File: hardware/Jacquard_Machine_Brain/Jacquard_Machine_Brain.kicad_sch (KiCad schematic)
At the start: 69 parts, among them J1 Terminal Block, J15 USB_A, J16 Wurth_RJ45_LED, J2 Conn_01x08, J3 JST-SH 01x04, J4 Conn_01x02, J5 Conn_01x02, SW1 SW_DIP_x02, SW2 SW_MEC_5G, U1 R-78E5.0-1.0, U10 74AHCT1G125, U2 Teensy4.1, U3 74AHCT1G125, U4 74AHCT1G125, U5 74AHCT125, U6 AO4882, U7 74AHCT1G125, U8 74AHCT1G125, U9 PCA9306D

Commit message: sync
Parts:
- removed C6: 0.1uF, Capacitor_SMD:C_0402_1005Metric, symbol Device:C_Small
- removed JP1, JP2, JP5, JP6, JP7, JP8: SolderJumper_2_Bridged, Jumper:SolderJumper-2_P1.3mm_Bridged_RoundedPad1.0x1.5mm, symbol Jumper:SolderJumper_2_Bridged
- removed R12, R13: 4.7k, Resistor_SMD:R_0603_1608Metric, symbol Device:R_Small
- removed U5: 74AHCT125, Package_SO:TSSOP-14_4.4x5mm_P0.65mm, symbol 0_integrated_circuits:74AHCT125_Multi
- added JP1, JP2, JP5: SolderJumper_3_Bridged123, Jumper:SolderJumper-3_P1.3mm_Bridged123_RoundedPad1.0x1.5mm_NumberLabels, symbol Jumper:SolderJumper_3_Bridged123
- added R17, R18, R19, R20: 4.7k, Resistor_SMD:R_0603_1608Metric, symbol Device:R_Small
- C9: value 0.1uF -> 100pF; LCSC C1525 -> C1546; Link https://www.digikey.com/en/products/detail/samsung-electro-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 -> (none); Manu # CL05B104KO5NNNC -> 0402CG101J500NT; Manu. Samsung Electro-Mechanics -> FH (Guangdong Fenghua Advanced Tech)
- U9: LCSC (none) -> C2677369
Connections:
- net +3V3: now also JP1.2 (C), JP2.2 (C)
- net +5V: now also JP5.2 (C); no longer R15.1, R16.1
- net GATE_1: now also R4.1
- net GATE_2: now also R5.1
- net SCL_0_3.3V: now also R19.2
- net SCL_0_5V: now also R15.2
- net SCL_1: now also R18.2
- net SDA_0_3.3V: now also R20.2
- net SDA_0_5V: now also R16.2
- net SDA_1: now also R17.2
- new net: JP1.1 (A), R18.1
- new net: JP1.3 (B), R17.1
- new net: JP2.1 (A), R20.1
- new net: JP2.3 (B), R19.1
- new net: JP5.1 (A), R16.1
- new net: JP5.3 (B), R15.1
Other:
- note added: "3.3V to 5V LEVEL CONVERSION FOR SHIFT REGISTER DRIVE"
- note added: "DUAL MOSFET SWITCHES"
- note added: "GP CONTROLS"
- note added: "MOSFET GATE DRIVE"
- note added: "TEENSY 4.1"
- moved on the sheet: C10, C11, C12, C3, C4, C5, C7, C8, C9, D2, D3, D4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

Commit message: Progress check
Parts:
- removed J16: Wurth_RJ45_LED, 0_connector:Wurth_7499010211A_RJ45, symbol 0_connector:Wurth_RJ45_LED
- removed JP2, JP5: SolderJumper_3_Bridged123, Jumper:SolderJumper-3_P1.3mm_Bridged123_RoundedPad1.0x1.5mm_NumberLabels, symbol Jumper:SolderJumper_3_Bridged123
- removed SW1: SW_DIP_x02, Button_Switch_THT:SW_DIP_SPSTx02_Slide_9.78x7.26mm_W7.62mm_P2.54mm, symbol Switch:SW_DIP_x02
- removed SW2: SW_MEC_5G, Button_Switch_THT:SW_TH_Tactile_Omron_B3F-100x, symbol Switch:SW_MEC_5G
- added C6: 0.1uF, Capacitor_SMD:C_0402_1005Metric, symbol Device:C_Small
- added J200: WIZnet_J1B1211CCD_RJ45, 0_connector:WIZnet_J1B1211CCD_RJ45, symbol 0_connector:WIZnet_J1B1211CCD_RJ45
- C3: footprint Capacitor_SMD:C_0805_2012Metric_Pad1.18x1.45mm_HandSolder -> Capacitor_SMD:C_0805_2012Metric; Digikey P/N (none) -> 311-1140-1-ND; Digikey Page (none) -> https://www.digikey.com/en/products/detail/yageo/CC0805KRX7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; LCSC (none) -> C49678; Link https://www.digikey.com/en/products/detail/samsung-electro-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 -> (none); Manu # CL21B104KBCNNNC -> CC0805KRX7R9BB104; Manu. Samsung Electro-Mechanics -> YAGEO
- F1: LCSC - -> C151075
- J1: LCSC - -> C89123
- J15: LCSC (none) -> C5815125
- JP1: footprint Jumper:SolderJumper-3_P1.3mm_Bridged123_RoundedPad1.0x1.5mm_NumberLabels -> Jumper:SolderJumper-3_P1.3mm_Open_RoundedPad1.0x1.5mm; symbol Jumper:SolderJumper_3_Bridged123 -> Jumper:SolderJumper_3_Open
- R3: value 330 -> 220R; footprint Resistor_SMD:R_0805_2012Metric_Pad1.20x1.40mm_HandSolder -> Resistor_SMD:R_0805_2012Metric; Digikey P/N (none) -> 311-220CRCT-ND; Digikey Page (none) -> https://www.digikey.com/en/products/detail/yageo/RC0805FR-0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; LCSC (none) -> C17557; Link https://mou.sr/4eszNXH -> (none); Manu # ERJ-P06J331V -> RC0805FR-07220RL; Manu. Panasonic -> YAGEO
- U1: LCSC - -> C22371890
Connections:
- net +3V3: now also R19.1, R20.1, C6.1
- net +5V: now also R15.1, R16.1
- net GND: now also C3.1, C6.2, J200.11, J200.8, J200.9; no longer C3.2
- net LATCH_3.3V: now also U2.43 (21_A7_RX5_BCLK1)
- net MOSFET_1: now also U2.32 (40_A16)
- net MOSFET_2: now also U2.33 (41_A17)
- net SERIAL_DATA_3.3V: now also U2.45 (23_A9_CRX1_MCLK1)
- net SRCLK_3.3V: now also U2.44 (22_A8_CTX1)
- net at R3.1: now also J200.12
- net at U2.63 (T+): now also J200.1
- net at U2.62 (T-): now also J200.3
- net at U2.60 (R+): now also J200.4
- net at U2.65 (R-): now also J200.6
- net at U2.61 (LED): now also J200.10
- net PWR_IN: now reaches F1.2, J1.1 (Pin_1)
- new net: C3.2, J200.2, J200.5
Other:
- note removed: "GP CONTROLS"
- moved on the sheet: C9, J2, JP3, JP4, R10, R15, R16, R19, R20, U9

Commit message: sync
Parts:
- removed J13: ~, Connector_PinSocket_2.54mm:PinSocket_1x04_P2.54mm_Vertical, symbol 0_connector:Molex Micro-Fit 4pos
- added J6: Conn_02x08_Odd_Even, Connector_PinSocket_2.54mm:PinSocket_2x08_P2.54mm_Vertical, symbol Connector_Generic:Conn_02x08_Odd_Even
- J2: LCSC (none) -> C42431840
- J4, J5: LCSC (none) -> C7499322
- R10: LCSC (none) -> C25764
- U2: LCSC (none) -> C41376163
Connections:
- net +3V3: now also U2.15 (3V3), J6.1 (Pin_1); no longer U2.46 (3V3)
- net +5V: now also J6.2 (Pin_2)
- net GND: now also J6.15 (Pin_15), J6.16 (Pin_16)
- net NIC_LED: now also U2.4 (2_OUT2); no longer U2.14 (12_MISO_MQSL)
- net SCL_1: now also U2.38 (16_A2_RX4_SCL1), J6.5 (Pin_5)
- net SDA_1: now also U2.39 (17_A3_TX4_SDA1), J6.3 (Pin_3)
- net SPI_CS: now reaches U2.12 (10_CS_MQSR)
- net SPI_CS: now also J6.4 (Pin_4)
- net SPI_MOSI: now reaches U2.13 (11_MOSI_CTX1)
- net SPI_MOSI: now also J6.6 (Pin_6)
- net UART_TX_6: now reaches U2.16 (24_A10_TX6_SCL2)
- net UART_TX_6: now also J6.12 (Pin_12)
- net UART_RX_6: now reaches U2.17 (25_A11_RX6_SDA2)
- net UART_RX_6: now also J6.14 (Pin_14)
- net GPIO_4: now reaches U2.28 (36_CS)
- net GPIO_4: now also J6.13 (Pin_13)
- net GPIO_3: now reaches U2.29 (37_CS)
- net GPIO_3: now also J6.11 (Pin_11)
- net GPIO_2: now reaches U2.30 (38_CS1_IN1)
- net GPIO_2: now also J6.9 (Pin_9)
- net GPIO_1: now reaches U2.31 (39_MISO1_OUT1A)
- net GPIO_1: now also J6.7 (Pin_7)
- net SPI_CLK: now reaches U2.35 (13_SCK_LED)
- net SPI_CLK: now also J6.10 (Pin_10)
- new net SPI_MISO: J6.8 (Pin_8), U2.14 (12_MISO_MQSL)
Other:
- note removed: "I2C"
- moved on the sheet: JP1, R17, R18

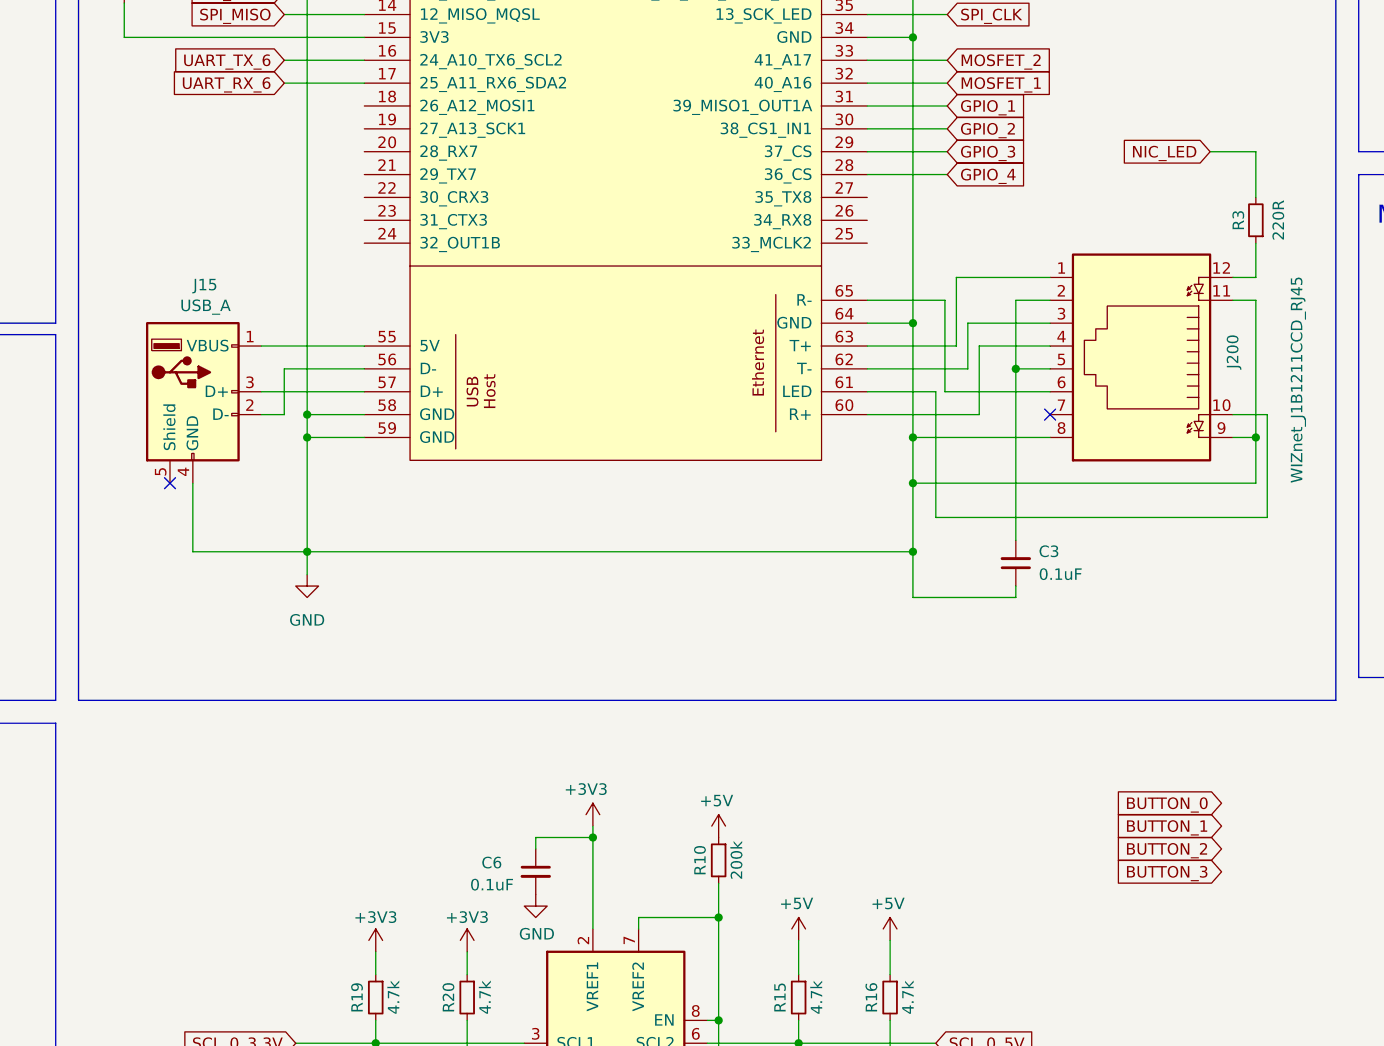
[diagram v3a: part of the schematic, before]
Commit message: Connected the UI buttons
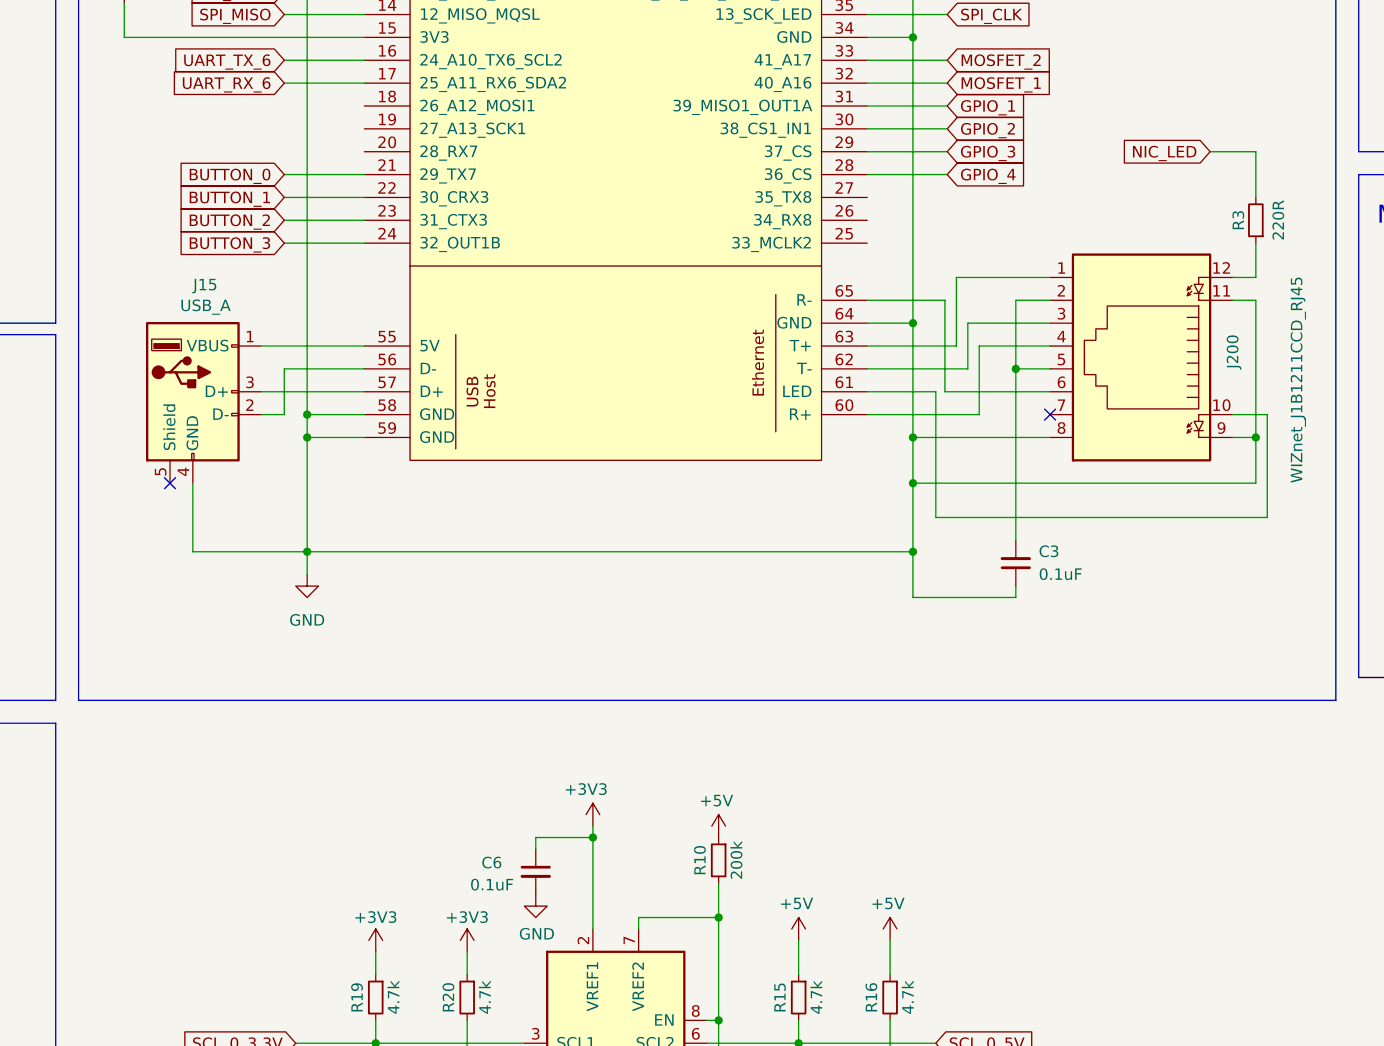
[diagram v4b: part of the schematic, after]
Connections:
- net BUTTON_0: now also U2.21 (29_TX7)
- net BUTTON_1: now also U2.22 (30_CRX3)
- net BUTTON_2: now also U2.23 (31_CTX3)
- net BUTTON_3: now also U2.24 (32_OUT1B)
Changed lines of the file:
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@@
+	(wire
+		(pts
+			(xy 127 86.36) (xy 135.89 86.36)
+		)
+		(stroke
+			(width 0)
+			(type default)
+		)
+	)
 	(wire
 		(pts
@@
 	(wire
 		(pts
+			(xy 127 81.28) (xy 135.89 81.28)
+		)
+		(stroke
+			(width 0)
+			(type default)
+		)
+	)
+	(wire
+		(pts
 			(xy 367.03 36.83) (xy 367.03 33.02)
 		)
@@
 	(wire
 		(pts
+			(xy 127 88.9) (xy 135.89 88.9)
+		)
+		(stroke
+			(width 0)
+			(type default)
+		)
+	)
+	(wire
+		(pts
 			(xy 229.87 78.74) (xy 234.95 78.74)
 		)
@@
 		(pts
 			(xy 383.54 123.19) (xy 396.24 123.19)
+		)
+		(stroke
+			(width 0)
+			(type default)
+		)
+	)
+	(wire
+		(pts
+			(xy 127 83.82) (xy 135.89 83.82)
 		)
 		(stroke
@@
 	(global_label "BUTTON_0"
 		(shape input)
-		(at 231.14 151.13 180)
-		(fields_autoplaced yes)
-		(effects
-			(font
-				(size 1.27 1.27)
-			)
-			(justify right)
-		)
-		(property "Intersheetrefs" "${INTERSHEET_REFS}"
-			(at 218.781 151.13 0)
+		(at 127 81.28 180)
+		(fields_autoplaced yes)
+		(effects
+			(font
+				(size 1.27 1.27)
+			)
+			(justify right)
+		)
+		(property "Intersheetrefs" "${INTERSHEET_REFS}"
+			(at 114.641 81.28 0)
 			(effects
 				(font
@@
 	(global_label "BUTTON_3"
 		(shape input)
-		(at 231.14 158.75 180)
-		(fields_autoplaced yes)
-		(effects
-			(font
-				(size 1.27 1.27)
-			)
-			(justify right)
-		)
-		(property "Intersheetrefs" "${INTERSHEET_REFS}"
-			(at 218.781 158.75 0)
+		(at 127 88.9 180)
+		(fields_autoplaced yes)
+		(effects
+			(font
+				(size 1.27 1.27)
+			)
+			(justify right)
+		)
+		(property "Intersheetrefs" "${INTERSHEET_REFS}"
+			(at 114.641 88.9 0)
 			(effects
 				(font
@@
 	(global_label "BUTTON_1"
 		(shape input)
-		(at 231.14 153.67 180)
-		(fields_autoplaced yes)
-		(effects
-			(font
-				(size 1.27 1.27)
-			)
-			(justify right)
-		)
-		(property "Intersheetrefs" "${INTERSHEET_REFS}"
-			(at 218.781 153.67 0)
+		(at 127 83.82 180)
+		(fields_autoplaced yes)
+		(effects
+			(font
+				(size 1.27 1.27)
+			)
+			(justify right)
+		)
+		(property "Intersheetrefs" "${INTERSHEET_REFS}"
+			(at 114.641 83.82 0)
 			(effects
 				(font
@@
 	(global_label "BUTTON_2"
 		(shape input)
-		(at 231.14 156.21 180)
-		(fields_autoplaced yes)
-		(effects
-			(font
-				(size 1.27 1.27)
-			)
-			(justify right)
-		)
-		(property "Intersheetrefs" "${INTERSHEET_REFS}"
-			(at 218.781 156.21 0)
-			(effects
-				(font
+		(at 127 86.36 180)
+		(fields_autoplaced yes)
+		(effects
+			(font
+				(size 1.27 1.27)
+			)
+			(justify right)
+		)
+		(property "Intersheetrefs" "${INTERSHEET_REFS}"
+			(at 114.641 86.36 0)
+			(effects
+				(font

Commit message: PCB Wrap up
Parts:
- C2: LCSC C50254 -> C377773
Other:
- note added: "CONNECTORS"
- note added: "I2C LOGIC CONVERSION"
- note added: "OPTIONAL: I2C_1 PULL-UPS"
- company: Meow Wolf -> Daniel Bornhorst
- title: (none) -> Jacuard Machine Brain
- moved on the sheet: J2, J3, J6, JP1, R11, R14, R17, R18, R2
